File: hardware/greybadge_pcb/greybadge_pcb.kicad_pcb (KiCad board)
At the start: 2 copper layers, 75 x 99 mm, 155 parts, among them J1 Conn_02x05_Row_Letter_First, J2 Conn_02x05_Row_Letter_First, J3 Conn_02x05_Row_Letter_First, J4 78171-0002, J5 USB_C_Receptacle_USB2.0, Q1 2N7002, Q2 Q_NMOS_GSD, SW1 SW_Push, SW10 SW_Push, SW2 SW_Push, SW3 SW_Push, SW4 SW_Push, SW5 SW_Push, SW6 SW_Push, SW7 SW_Push, SW8 SW_SPST, SW9 SW_Push, U10 AMS1117-3.3, U2 TLV73311PDBV, U3 TLV73325PDBV, U4 GC9A01_IPS_display, U5 BQ24075, U6 W25Q128JVS, U7 RP2350_60QFN, U8 ECP5U_25_CABGA256, U9 W25Q128JVSIM, X1 SiT2001B, Y1 12Mhz

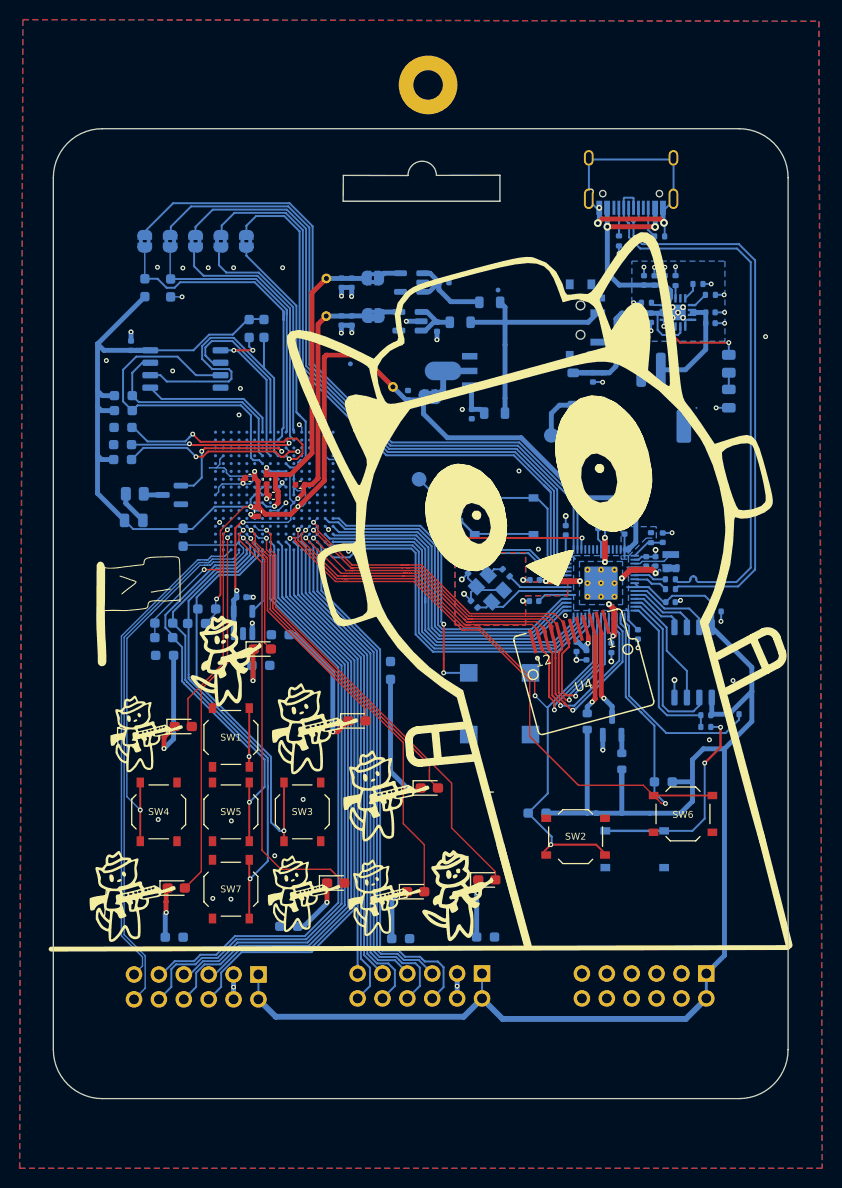
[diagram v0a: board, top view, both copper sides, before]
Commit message: Route ADC and power, cleanup routing/silkscreen
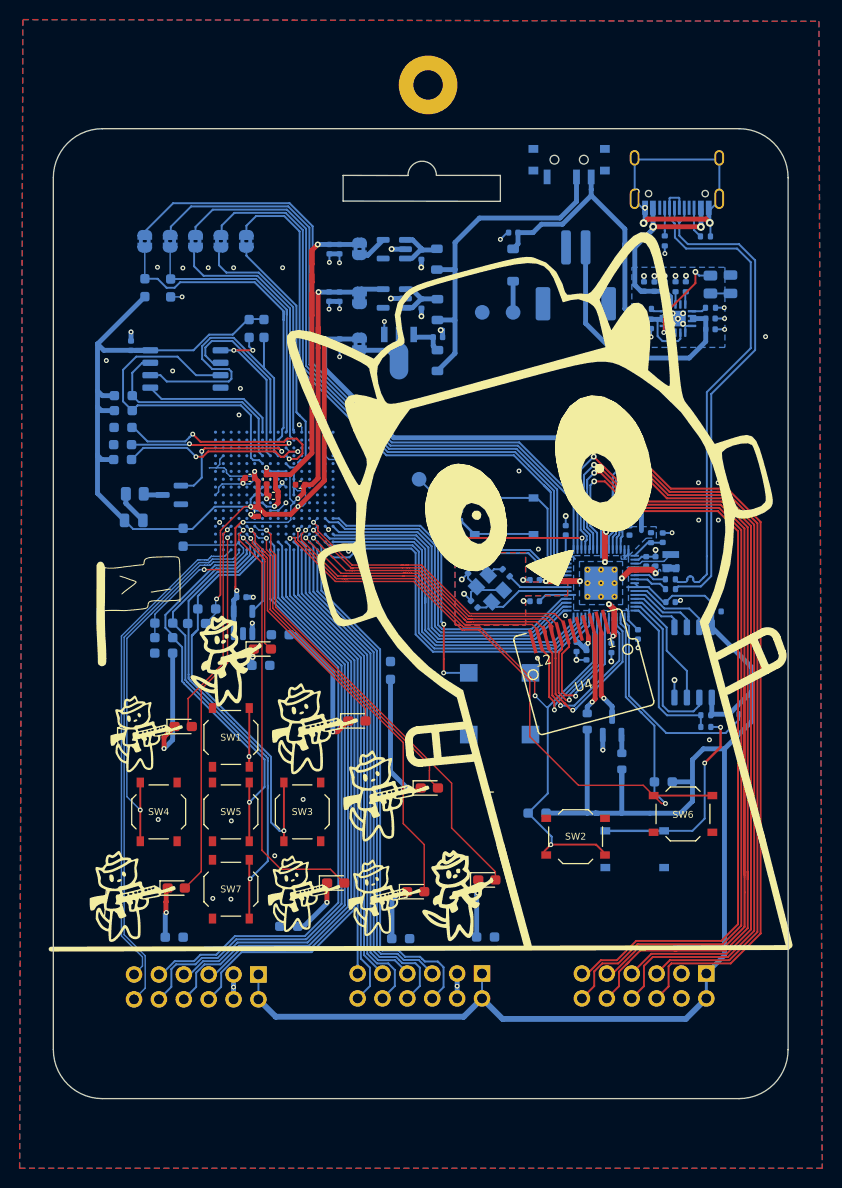
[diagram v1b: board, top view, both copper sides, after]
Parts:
- removed TP1: F1V1, TestPoint:TestPoint_THTPad_D1.0mm_Drill0.5mm
- removed TP2: F3V3, TestPoint:TestPoint_THTPad_D1.0mm_Drill0.5mm
- removed TP3: F2V5, TestPoint:TestPoint_THTPad_D1.0mm_Drill0.5mm
- moved C17 16.9 mm to (128.7, 61.6), turned to 180 degrees
- moved AA-1 16.4 mm to (125.5, 69.7), turned to 90 degrees
- moved SW8 16.1 mm to (134.4, 54.5), turned to 0 degrees
- moved J4 14.7 mm to (135.1, 66.0)
- moved D10 14.1 mm to (128.7, 64.9)
- moved AA+1 13.1 mm to (128.7, 69.7), turned to 90 degrees
- moved D9 11.7 mm to (150.9, 66.9), turned to -90 degrees
- moved JP7 8.98 mm to (113.0, 73.0), turned to 90 degrees
- moved C11 8.74 mm to (111.0, 72.9), turned to -90 degrees
- moved C3 8.57 mm to (121.0, 72.3), turned to 0 degrees
- moved R20 8.30 mm to (148.8, 66.9)
- moved FB2 7.93 mm to (121.0, 74.6), turned to -90 degrees
- moved FB1 6.97 mm to (120.9, 64.3), turned to -90 degrees
- moved U10 6.32 mm to (117.0, 73.3), turned to 90 degrees
- moved R35 4.67 mm to (144.2, 62.4)
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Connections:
- J3 pad 10: unconnected-(J3-Pin_10-Pad10) -> GPIO22
- J3 pad 11: unconnected-(J3-Pin_11-Pad11) -> GPIO25
- J3 pad 12: unconnected-(J3-Pin_12-Pad12) -> GPIO24
- J3 pad 5: unconnected-(J3-Pin_5-Pad5) -> GPIO27
- J3 pad 6: unconnected-(J3-Pin_6-Pad6) -> GPIO26
- J3 pad 7: unconnected-(J3-Pin_7-Pad7) -> GPIO29
- J3 pad 8: unconnected-(J3-Pin_8-Pad8) -> GPIO28
- J3 pad 9: unconnected-(J3-Pin_9-Pad9) -> GPIO23
- SW8 pad 1: /EN1 -> unconnected-(SW8-A-Pad1)
- SW8 pad 3: unconnected-(SW8-C-Pad3) -> /EN1
- U7 pad 40: /rp2350/GPIO26_ADC0 -> GPIO26
- U7 pad 41: /rp2350/GPIO27_ADC1 -> GPIO27
- U7 pad 42: /rp2350/GPIO28_ADC2 -> GPIO28
- U7 pad 43: /rp2350/GPIO29_ADC3 -> GPIO29
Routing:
- net GPIO23: track 0.00 -> 114.0 mm, vias 0 -> 1
- net GPIO22: track 0.00 -> 89.5 mm, vias 0 -> 1
- net GPIO24: track 0.00 -> 87.1 mm, vias 0 -> 1
- net GPIO26: track 0.00 -> 85.3 mm, vias 0 -> 1
- net GPIO25: track 0.00 -> 82.3 mm, vias 0 -> 1
- net GPIO28: track 0.00 -> 81.6 mm, vias 0 -> 1
- net GPIO27: track 0.00 -> 80.2 mm, vias 0 -> 1
- net GPIO29: track 0.00 -> 78.3 mm, vias 0 -> 1
- net +BATT: track 11.0 -> 26.3 mm
- net /EN1: track 26.0 -> 36.4 mm
- net +Vout: track 24.9 -> 34.2 mm
- net +3V3: track 358.4 -> 367.4 mm, vias 6 -> 7
- net +F1V1: track 37.1 -> 44.9 mm, vias 2 -> 3
- net /rp2350/USB_D-: track 59.9 -> 53.0 mm
- net /rp2350/USB_D+: track 58.4 -> 51.5 mm
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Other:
- outline, holes or cut-outs redrawn
- board text added: "1V1"
- board text added: "SWCLK"
- board text added: "SWD"

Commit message: Remove collinear tracks
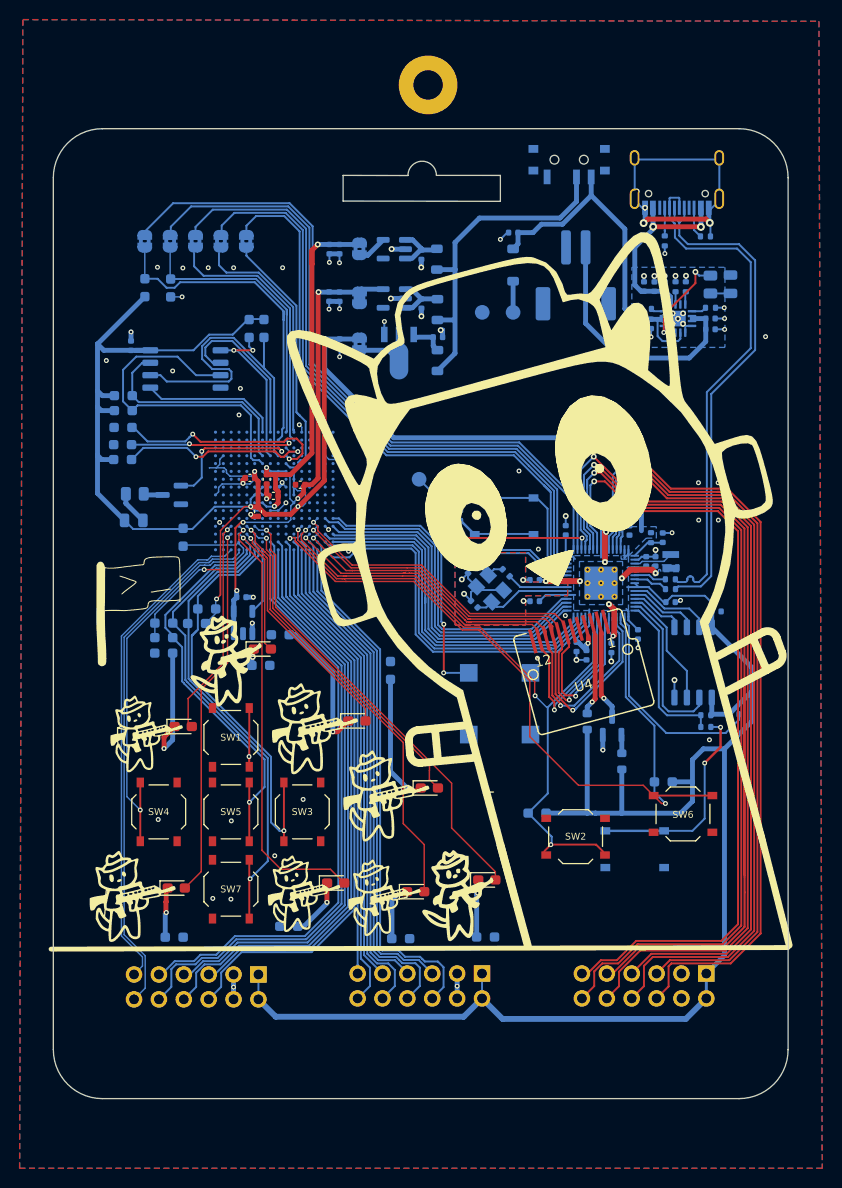
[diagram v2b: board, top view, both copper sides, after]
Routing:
- net +F1V1: track 44.9 -> 41.7 mm
- net +3V3: track 367.4 -> 364.6 mm
- net GPIO26: track 85.3 -> 83.3 mm
- net GPIO22: track 89.5 -> 88.2 mm
- net GPIO29: track 78.3 -> 77.1 mm
- net +F2V5: track 57.3 -> 56.3 mm
- net +5V_USB: track 21.0 -> 20.0 mm
- net /EN1: track 36.4 -> 35.6 mm
- net GPIO27: track 80.2 -> 79.6 mm

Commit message: Update font sizes
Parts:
- moved G*** 2.55 mm to (149.0, 123.0)
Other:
- board text added: "github.com/NUSGreyhats pcb: hackin7 & itsme-zeix art: shuqing"

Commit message: feat: saf section
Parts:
- removed the G*** at (123.3, 129.3)
- removed the G*** at (89.9, 129.3)
- removed the G*** at (108.5, 112.2)
- removed the G*** at (115.8, 119.0)
- removed the G*** at (99.7, 105.4)
- added G***: LOGO, LOGO, F.Cu at (108.2, 113.5)
- added G***: LOGO, LOGO, F.Cu at (118.9, 129.0)
- added G***: LOGO, LOGO, F.Cu at (115.5, 120.0)
- added G***: LOGO, LOGO, F.Cu at (98.4, 105.9)
- moved G*** 25.0 mm to (90.6, 129.0)
- moved D4 9.06 mm to (120.2, 119.9)
- moved D7 2.61 mm to (123.5, 126.9)
- moved D5 1.65 mm to (103.0, 102.4)
- moved G*** 0.56 mm to (107.7, 128.6)
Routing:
- net Net-(D4-K): track 5.87 -> 15.0 mm
- net D5: track 44.8 -> 36.5 mm
- net D6: track 46.7 -> 44.9 mm
- net Net-(D7-K): track 5.89 -> 7.59 mm
- net C4: track 13.1 -> 11.4 mm
- net Net-(D5-K): track 1.80 -> 3.44 mm

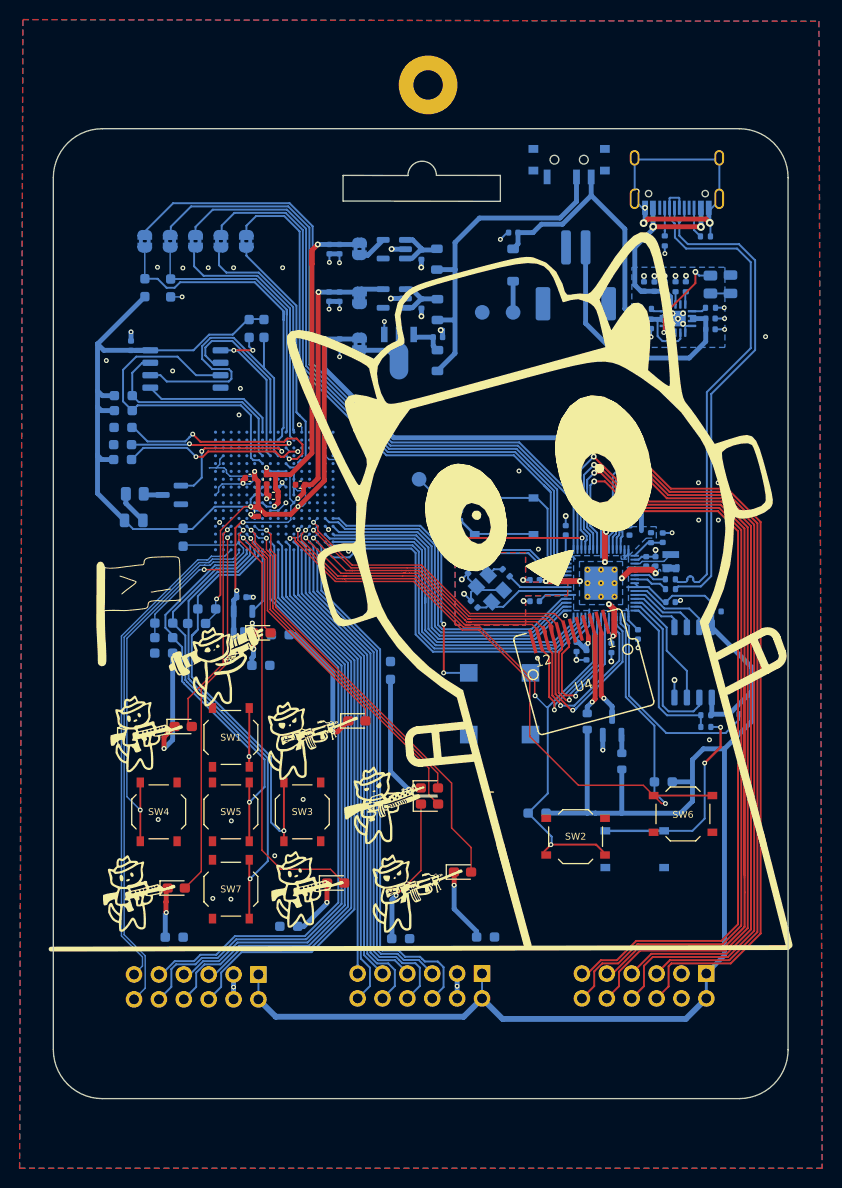
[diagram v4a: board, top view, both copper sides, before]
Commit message: feat: back silkscreen
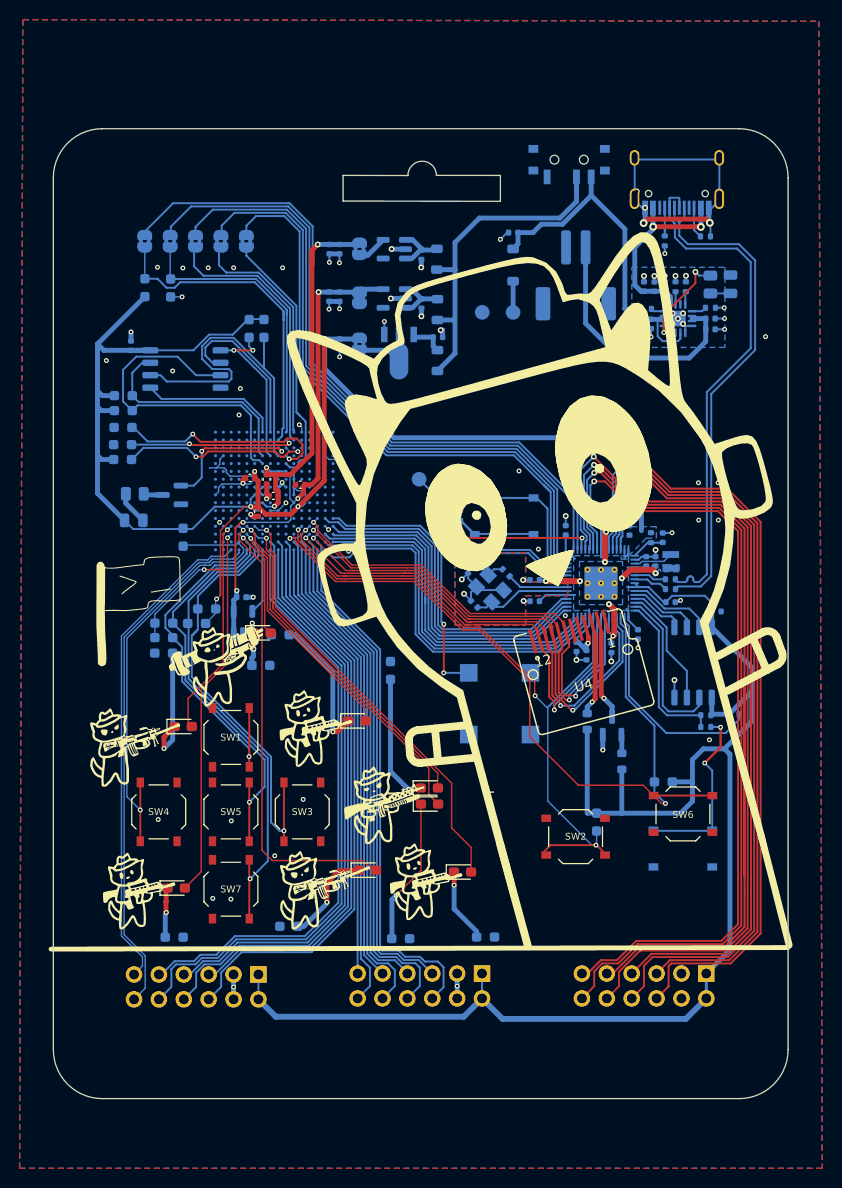
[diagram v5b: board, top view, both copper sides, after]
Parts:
- removed the G*** at (108.7, 115.7)
- removed the G*** at (95.5, 115.7)
- removed H1: MountingHole, MountingHole:MountingHole_3mm_Pad
- moved G*** 43.1 mm to (149.5, 79.9)
- moved G*** 18.2 mm to (90.1, 114.1)
- moved G*** 17.3 mm to (108.6, 112.2)
- moved G*** 12.1 mm to (119.8, 127.8)
- moved G*** 9.45 mm to (109.4, 128.7)
- moved R3 6.14 mm to (137.2, 121.8), turned to -90 degrees
- moved SW9 4.91 mm to (146.0, 124.5)
- moved D8 3.50 mm to (113.8, 126.7)
- moved G*** 0.25 mm to (90.6, 128.7)
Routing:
- net Net-(D8-K): track 6.04 -> 9.83 mm
- net +3V3: track 364.6 -> 360.9 mm
- net /rp2350/~{USB_BOOT}: track 21.6 -> 18.5 mm
- net D4: track 44.2 -> 46.9 mm
- net D12: track 68.6 -> 70.4 mm
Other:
- board text added: "3.3V, GND, 27, 29, 23, 25 3.3V, GND, 26, 28, 22, 24"
- board text added: "3.3V, GND, A10, A9, A8, A3 3.3V, GND, B10, B9, B8, A4"
- board text added: "3.3V, GND, A14, A13, A12, A11 3.3V, GND, B14, B13, B12, B11"
- board text added: "Army/ ECP5"
- board text added: "GP20/crst GP19/tck GP18/tdi GP17/tms GP16/tdo"
- board text added: "JTAG"
- board text added: "Mecha/ RP2350"
- board text added: "PMOD ECP5"
- board text added: "PMOD RP2350"
